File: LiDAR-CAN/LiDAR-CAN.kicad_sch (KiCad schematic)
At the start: 15 parts, among them J1 G7LX-A88S7-BP-G/Y

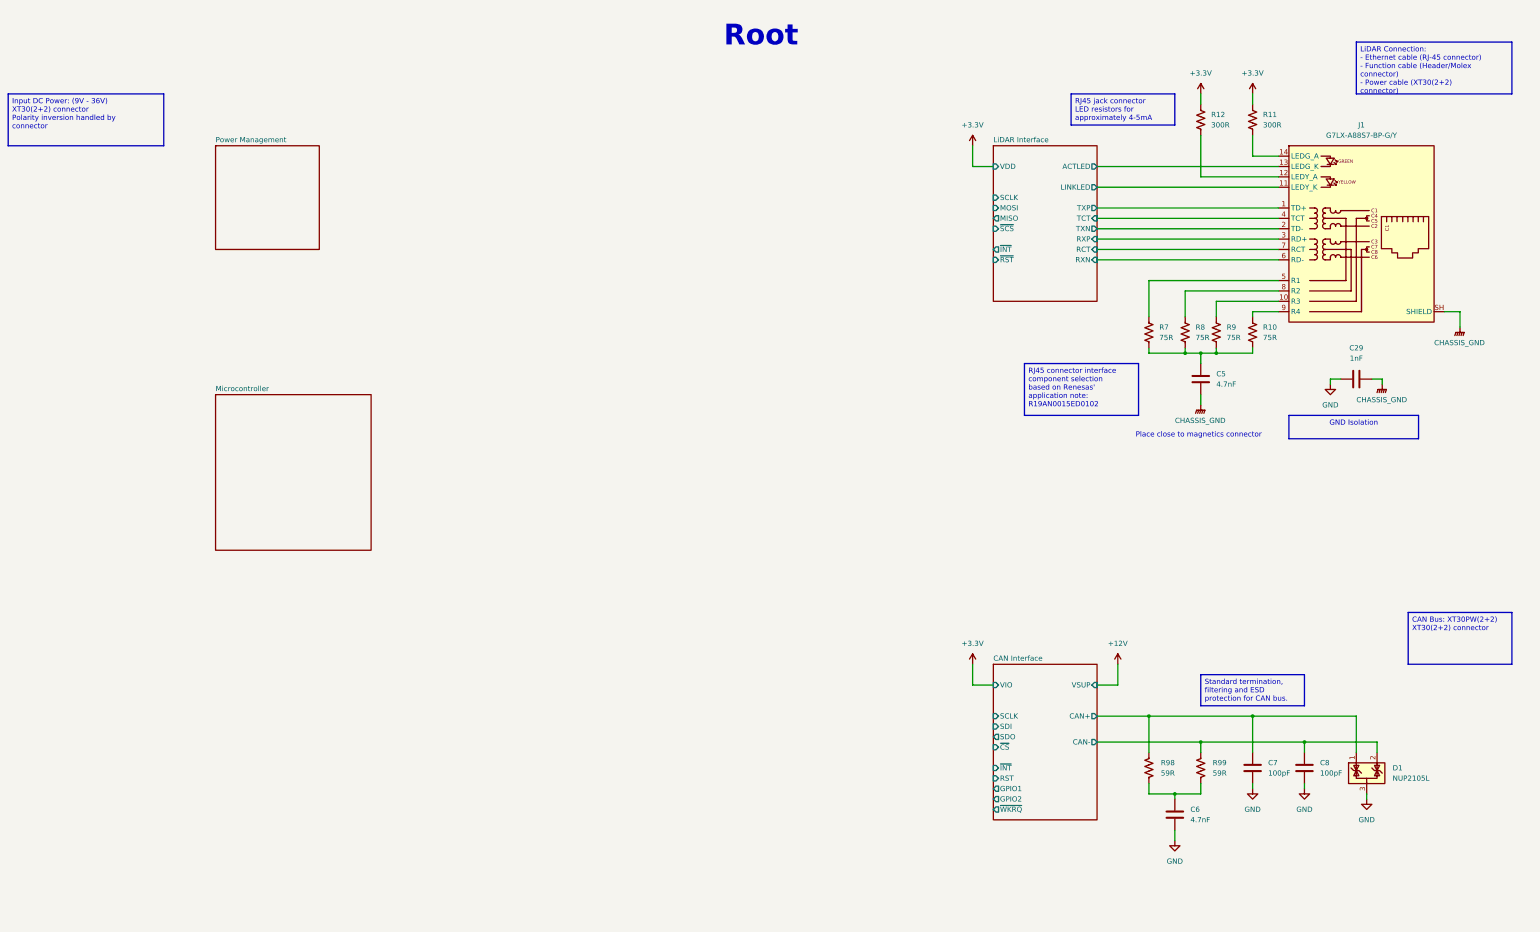
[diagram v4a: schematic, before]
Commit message: Add MCU connections in root sheet
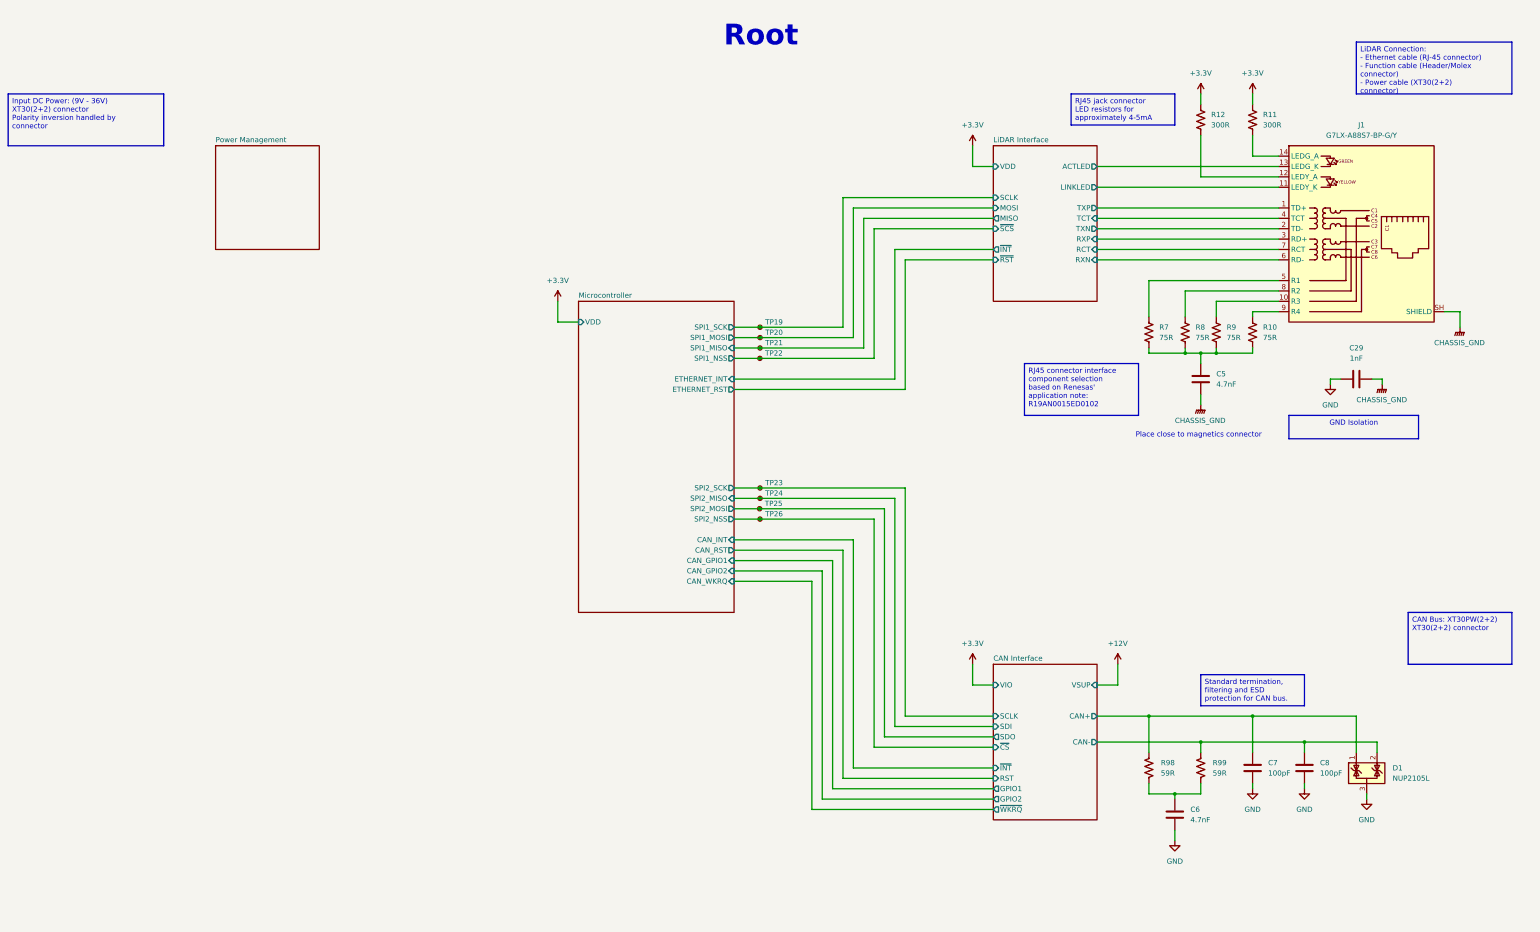
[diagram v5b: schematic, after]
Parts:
- added TP19, TP20, TP21, TP22, TP23, TP24, TP25, TP26: TestPoint_Small, TestPoint:TestPoint_Pad_D1.0mm, symbol Connector:TestPoint_Small
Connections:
- net CAN Interface/SCLK: now also TP23.1
- net CAN Interface/SDI: now also TP24.1
- net CAN Interface/SDO: now also TP25.1
- net CAN Interface/~{CS}: now also TP26.1
- net LiDAR Interface/MISO: now also TP21.1
- net LiDAR Interface/MOSI: now also TP20.1
- net LiDAR Interface/SCLK: now also TP19.1
- net LiDAR Interface/~{SCS}: now also TP22.1
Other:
- sheet Microcontroller ports: added CAN_GPIO1, CAN_GPIO2, CAN_INT, CAN_RST, CAN_WKRQ, ETHERNET_INT, ETHERNET_RST, SPI1_MISO, SPI1_MOSI, SPI1_NSS, SPI1_SCK, SPI2_MISO, SPI2_MOSI, SPI2_NSS, SPI2_SCK, VDD; removed none

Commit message: Add power management connections in Root sheet
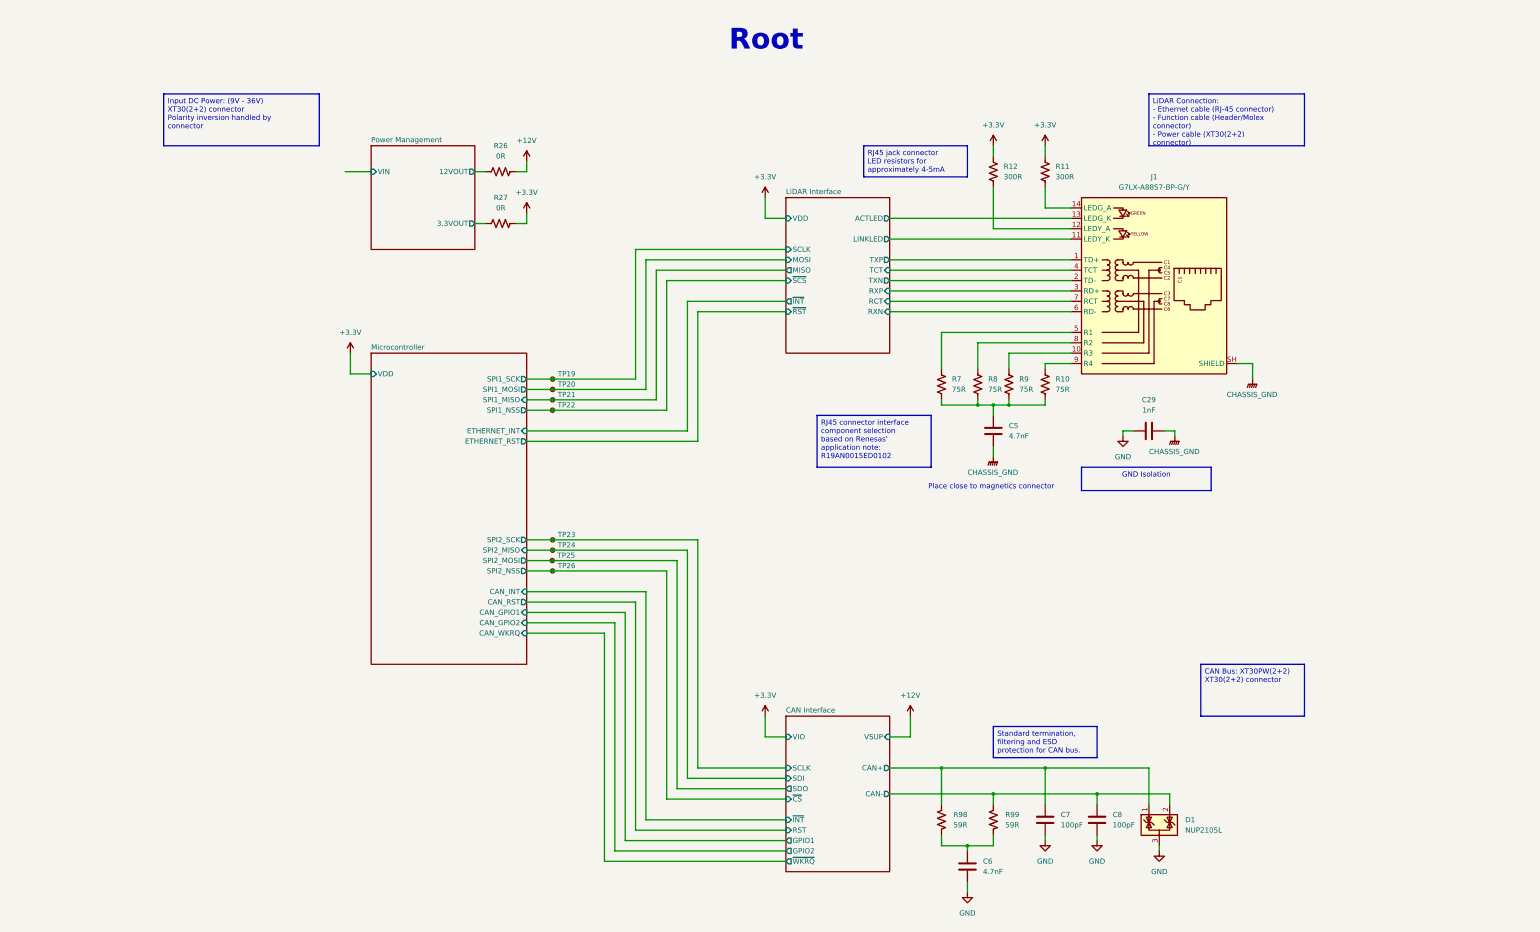
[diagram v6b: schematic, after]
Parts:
- added R26, R27: 0R, Resistor_SMD:R_0805_2012Metric, symbol Device:R_US
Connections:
- net +12V: now also R26.2
- net +3.3V: now also R27.2
- new net Power Management/12VOUT: R26.1
- new net Power Management/3.3VOUT: R27.1
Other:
- sheet Power Management ports: added 12VOUT, 3.3VOUT, VIN; removed none
- moved on the sheet: C29, C5, C6, C7, C8, D1, J1, R10, R11, R12, R7, R8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

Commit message: Feature schematic revision 1
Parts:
- added FID1, FID2: Fiducial, Fiducial:Fiducial_1.5mm_Mask3mm, symbol Mechanical:Fiducial
- added H1, H2: MountingHole, MountingHole:MountingHole_2.2mm_M2, symbol Mechanical:MountingHole
- added J1, J2, J4: XT30(2+2), symbol Connector_Generic:Conn_01x04
- C2: renamed from C29; footprint 1000 pF ±20% 2000V (2kV) Ceramic Capacitor X7R 1808 (4520 Metric) -> Capacitor_SMD:C_1808_4520Metric
- renumbered C5 to C1, C7 to C3, C8 to C4, C6 to C5, J1 to J3, R26 to R1, R99 to R10, R27 to R2, R12 to R3, R11 to R4, R7 to R5, R8 to R6, R9 to R7, R10 to R8, R98 to R9, TP19 to TP1, TP20 to TP2, TP21 to TP3, TP22 to TP4, TP23 to TP5, TP24 to TP6, TP25 to TP7, TP26 to TP8
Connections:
- net +12V: now also J1.1 (Pin_1)
- net CAN Interface/CAN+: now also J4.1 (Pin_1)
- net CAN Interface/CAN-: now also J4.2 (Pin_2)
- net GND: now also J1.2 (Pin_2), J2.2 (Pin_2)
- net Power Management/VIN: now also J2.1 (Pin_1)
- no-connect marks 0 -> 6
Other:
- moved on the sheet: C1, C2, J3, R3, R4, R5, R6, R7, R8, TP1, TP2, TP3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

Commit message: Start placement of components
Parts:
- J1, J2, J4: footprint (none) -> Local_Library:XT30PW(2+2)-M.G.B
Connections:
- net CAN Interface/CAN+: now also D1.2 (K), J4.2 (Pin_2); no longer D1.1 (K), J4.1 (Pin_1)
- net CAN Interface/CAN-: now also D1.1 (K), J4.1 (Pin_1); no longer D1.2 (K), J4.2 (Pin_2)
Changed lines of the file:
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@@
 	)
 	(junction
-		(at 309.88 209.55)
+		(at 260.35 222.25)
 		(diameter 0)
 		(color 0 0 0 0)
 	)
 	(junction
-		(at 260.35 222.25)
+		(at 158.75 123.19)
 		(diameter 0)
 		(color 0 0 0 0)
 	)
 	(junction
-		(at 158.75 123.19)
+		(at 309.88 203.2)
 		(diameter 0)
 		(color 0 0 0 0)
@@
 	)
 	(junction
-		(at 304.8 203.2)
+		(at 254 203.2)
 		(diameter 0)
 		(color 0 0 0 0)
 	)
 	(junction
-		(at 254 203.2)
+		(at 158.75 165.1)
 		(diameter 0)
 		(color 0 0 0 0)
 	)
 	(junction
-		(at 158.75 165.1)
+		(at 304.8 209.55)
 		(diameter 0)
 		(color 0 0 0 0)
@@
 	(wire
 		(pts
+			(xy 332.74 205.74) (xy 342.9 205.74)
+		)
+		(stroke
+			(width 0)
+			(type default)
+		)
+	)
+	(wire
+		(pts
 			(xy 266.7 137.16) (xy 266.7 139.7)
 		)
@@
 	(wire
 		(pts
-			(xy 317.5 209.55) (xy 309.88 209.55)
-		)
-		(stroke
-			(width 0)
-			(type default)
-		)
-	)
-	(wire
-		(pts
 			(xy 215.9 220.98) (xy 176.53 220.98)
 		)
@@
 	(wire
 		(pts
+			(xy 304.8 209.55) (xy 304.8 212.09)
+		)
+		(stroke
+			(width 0)
+			(type default)
+		)
+	)
+	(wire
+		(pts
 			(xy 266.7 209.55) (xy 266.7 212.09)
 		)
@@
 	(wire
 		(pts
-			(xy 342.9 205.74) (xy 317.5 205.74)
+			(xy 194.31 160.02) (xy 158.75 160.02)
 		)
 		(stroke
@@
 	(wire
 		(pts
-			(xy 194.31 160.02) (xy 158.75 160.02)
+			(xy 215.9 215.9) (xy 181.61 215.9)
 		)
 		(stroke
@@
 	(wire
 		(pts
-			(xy 304.8 203.2) (xy 304.8 212.09)
+			(xy 176.53 220.98) (xy 176.53 177.8)
 		)
 		(stroke
@@
 	(wire
 		(pts
-			(xy 215.9 215.9) (xy 181.61 215.9)
+			(xy 266.7 83.82) (xy 266.7 73.66)
 		)
 		(stroke
@@
 	(wire
 		(pts
-			(xy 176.53 220.98) (xy 176.53 177.8)
+			(xy 215.9 208.28) (xy 189.23 208.28)
 		)
 		(stroke
@@
 	(wire
 		(pts
-			(xy 266.7 83.82) (xy 266.7 73.66)
+			(xy 152.4 167.64) (xy 158.75 167.64)
 		)
 		(stroke
@@
 	(wire
 		(pts
-			(xy 215.9 208.28) (xy 189.23 208.28)
+			(xy 332.74 203.2) (xy 330.2 205.74)
 		)
 		(stroke
@@
 	(wire
 		(pts
-			(xy 152.4 167.64) (xy 158.75 167.64)
+			(xy 191.77 101.6) (xy 215.9 101.6)
 		)
 		(stroke
@@
 	(wire
 		(pts
-			(xy 191.77 101.6) (xy 215.9 101.6)
+			(xy 152.4 180.34) (xy 173.99 180.34)
 		)
 		(stroke
@@
 	(wire
 		(pts
-			(xy 152.4 180.34) (xy 173.99 180.34)
+			(xy 304.8 43.18) (xy 304.8 50.8)
 		)
 		(stroke
@@
 	(wire
 		(pts
-			(xy 304.8 43.18) (xy 304.8 50.8)
+			(xy 304.8 209.55) (xy 317.5 209.55)
 		)
 		(stroke
@@
 	(wire
 		(pts
-			(xy 292.1 209.55) (xy 309.88 209.55)
+			(xy 292.1 209.55) (xy 304.8 209.55)
+		)
+		(stroke
+			(width 0)
+			(type default)
+		)
+	)
+	(wire
+		(pts
+			(xy 342.9 203.2) (xy 332.74 203.2)
 		)
 		(stroke
@@
 	(wire
 		(pts
+			(xy 309.88 203.2) (xy 309.88 212.09)
+		)
+		(stroke
+			(width 0)
+			(type default)
+		)
+	)
+	(wire
+		(pts
+			(xy 330.2 203.2) (xy 332.74 205.74)
+		)
+		(stroke
+			(width 0)
+			(type default)
+		)
+	)
+	(wire
+		(pts
 			(xy 101.6 59.69) (xy 101.6 62.23)
 		)
@@
 	(wire
 		(pts
-			(xy 304.8 203.2) (xy 342.9 203.2)
-		)
-		(stroke
-			(width 0)
-			(type default)
-		)
-	)
-	(wire
-		(pts
 			(xy 186.69 96.52) (xy 215.9 96.52)
 		)
@@
 	(wire
 		(pts
+			(xy 317.5 205.74) (xy 330.2 205.74)
+		)
+		(stroke
+			(width 0)
+			(type default)
+		)
+	)
+	(wire
+		(pts
 			(xy 241.3 104.14) (xy 285.75 104.14)
 		)
@@
 	(wire
 		(pts
-			(xy 279.4 219.71) (xy 279.4 220.98)
+			(xy 309.88 203.2) (xy 330.2 203.2)
 		)
 		(stroke
@@
 	(wire
 		(pts
-			(xy 254 127) (xy 262.89 127)
+			(xy 279.4 219.71) (xy 279.4 220.98)
 		)
 		(stroke
@@
 	(wire
 		(pts
-			(xy 279.4 203.2) (xy 304.8 203.2)
+			(xy 254 127) (xy 262.89 127)
 		)
 		(stroke
@@
 	(wire
 		(pts
-			(xy 309.88 209.55) (xy 309.88 212.09)
+			(xy 292.1 209.55) (xy 292.1 212.09)
 		)
 		(stroke
@@
 	(wire
 		(pts
-			(xy 292.1 209.55) (xy 292.1 212.09)
+			(xy 88.9 57.15) (xy 114.3 57.15)
 		)
 		(stroke
@@
 	(wire
 		(pts
-			(xy 88.9 57.15) (xy 114.3 57.15)
+			(xy 194.31 203.2) (xy 194.31 160.02)
 		)
 		(stroke
@@
 	(wire
 		(pts
-			(xy 194.31 203.2) (xy 194.31 160.02)
+			(xy 152.4 69.85) (xy 149.86 69.85)
 		)
 		(stroke
@@
 	(wire
 		(pts
-			(xy 152.4 69.85) (xy 149.86 69.85)
+			(xy 210.82 195.58) (xy 215.9 195.58)
 		)
 		(stroke
@@
 	(wire
 		(pts
-			(xy 210.82 195.58) (xy 215.9 195.58)
+			(xy 279.4 203.2) (xy 309.88 203.2)
 		)
 		(stroke
@@
 		(exclude_from_sim no)
 		(in_bom no)
-		(on_board no)
+		(on_board yes)
 		(dnp no)
 		(fields_autoplaced yes)
@@
 		(exclude_from_sim no)
 		(in_bom no)
-		(on_board no)
+		(on_board yes)
 		(dnp no)
 		(fields_autoplaced yes)
@@
 		(exclude_from_sim no)
 		(in_bom no)
-		(on_board no)
+		(on_board yes)
 		(dnp no)
 		(fields_autoplaced yes)
@@
 		(exclude_from_sim no)
 		(in_bom no)
-		(on_board no)
+		(on_board yes)
 		(dnp no)
 		(fields_autoplaced yes)
@@
 			)
 		)
-		(property "Footprint" ""
+		(property "Footprint" "Local_Library:XT30PW(2+2)-M.G.B"
 			(at 347.98 205.74 0)
 			(effects
@@
 			)
 		)
-		(property "Footprint" ""
+		(property "Footprint" "Local_Library:XT30PW(2+2)-M.G.B"
 			(at 83.82 59.69 0)
 			(effects
@@
 			)
 		)
-		(property "Footprint" ""
+		(property "Footprint" "Local_Library:XT30PW(2+2)-M.G.B"
 			(at 316.23 43.18 0)
 			(effects
@@
 		(exclude_from_sim no)
 		(in_bom no)
-		(on_board no)
+		(on_board yes)
 		(dnp no)
 		(fields_autoplaced yes)
@@
 		(exclude_from_sim no)
 		(in_bom no)
-		(on_board no)
+		(on_board yes)
 		(dnp no)
 		(fields_autoplaced yes)
@@
 		(exclude_from_sim no)
 		(in_bom no)
-		(on_board no)
+		(on_board yes)
 		(dnp no)
 		(fields_autoplaced yes)
@@
 		(exclude_from_sim no)
 		(in_bom no)
-		(on_board no)
+		(on_board yes)
 		(dnp no)
 		(fields_autoplaced yes)
